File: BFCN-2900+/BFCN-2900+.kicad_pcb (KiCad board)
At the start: 2 copper layers, 60 x 30 mm, 7 parts, among them U1 BFCN-2900+, X1 SMA-BU, X2 SMA-BU

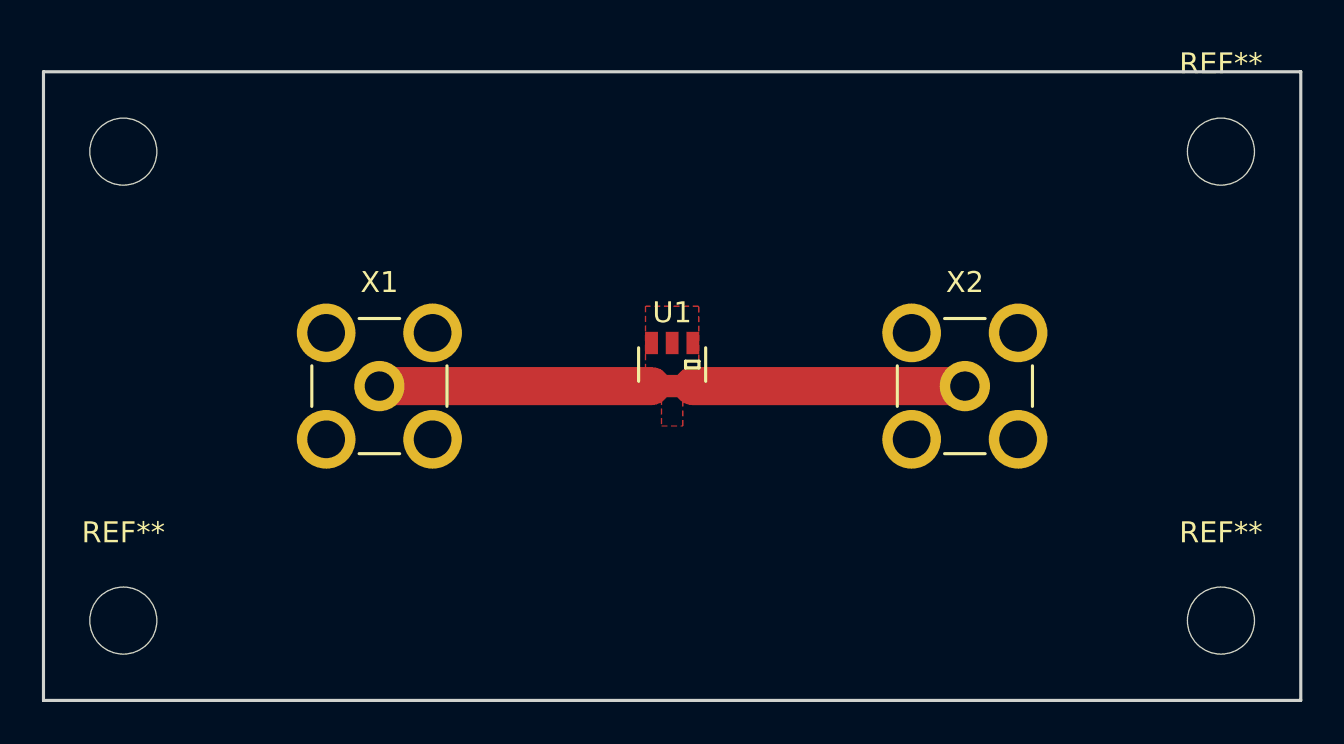
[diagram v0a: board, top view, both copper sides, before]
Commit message: BFCN-2900+: Removed thermals
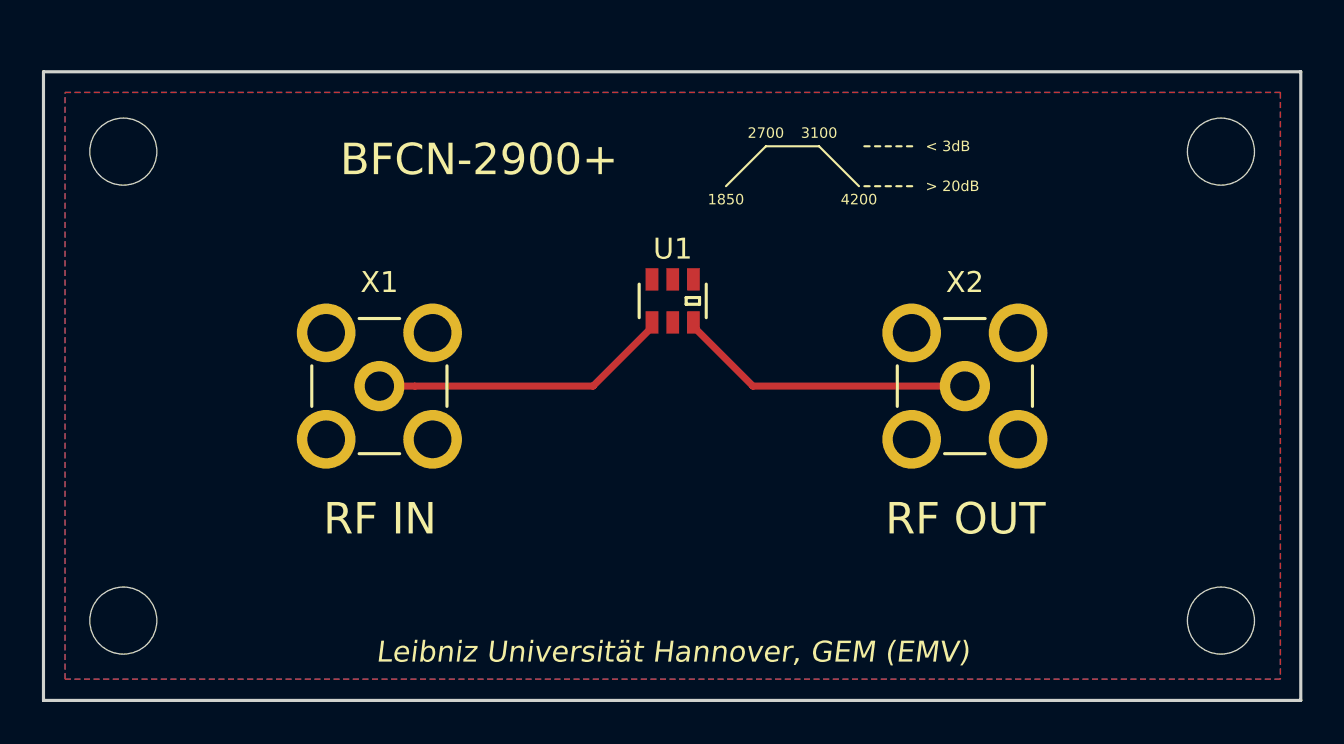
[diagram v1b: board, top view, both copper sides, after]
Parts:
- moved U1 3.04 mm to (120.0, 100.9)
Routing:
- net Net-(U1-Pad1): track 13.0 -> 14.4 mm
- net Net-(U1-Pad3): track 13.0 -> 14.3 mm
- added copper zone on B.Cu, net GNDA
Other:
- net class 50Ohm: clearance 0.1 -> 0.2; trace_width 1.82 -> 0.336; via_dia 0.6 -> 0.4; via_drill 0.4 -> 0.3
- net class Default: clearance 0.2 -> 0.1; trace_width 0.25 -> 0.15; via_dia 0.6 -> 0.4; via_drill 0.4 -> 0.3
- rule trace_clearance: 0.2 -> 0.1
- rule trace_min: 0.2 -> 0.15
- board text added: "1850"
- board text added: "2700"
- board text added: "3100"
- board text added: "4200"
- board text added: "< 3dB"
- board text added: "> 20dB"
- board text added: "BFCN-2900+"
- board text added: "Leibniz Universität Hannover, GEM (EMV)"
- board text added: "RF IN"
- board text added: "RF OUT"

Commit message: BFCN-2900+: Some vias, new footprints
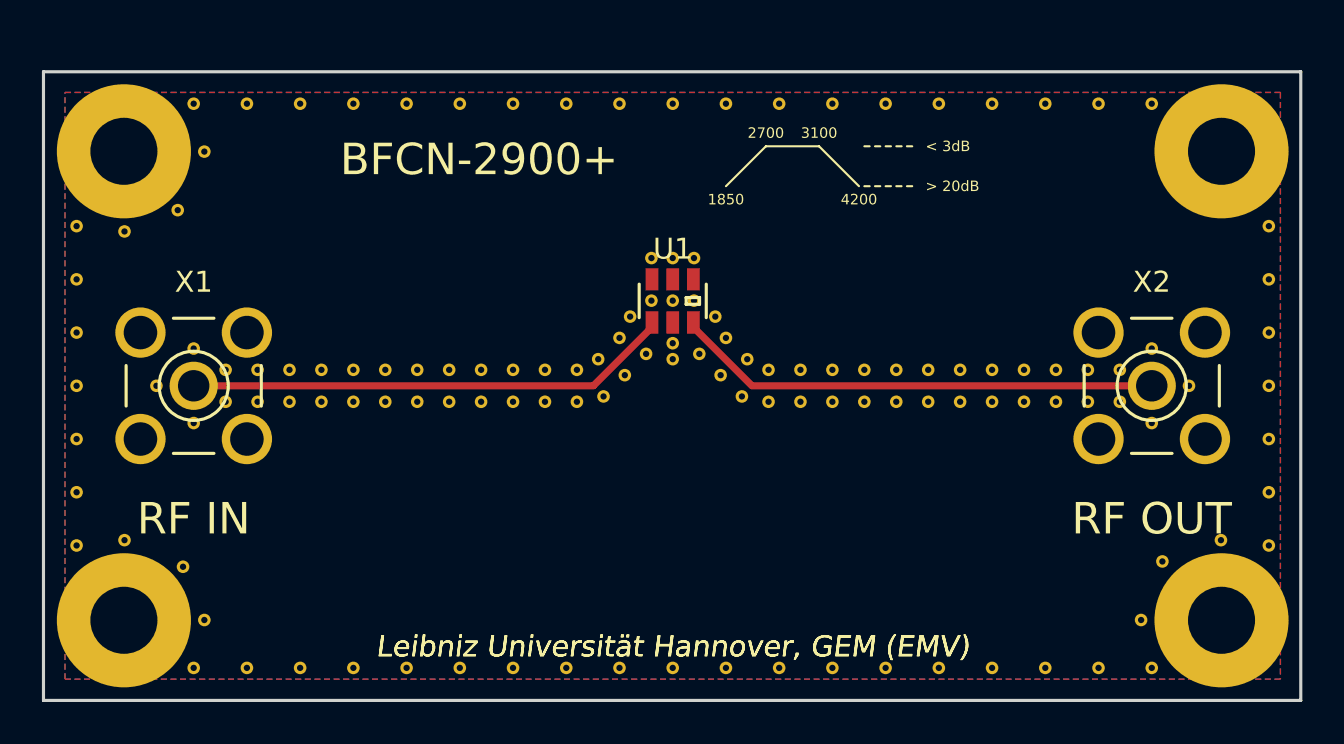
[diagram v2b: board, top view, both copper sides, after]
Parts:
- removed the REF** at (146.2, 93.8)
- removed the REF** at (146.2, 116.2)
- removed the REF** at (93.8, 93.8)
- removed the REF** at (93.8, 116.2)
- added REF**: VIA-0.3, JueVias:VIA-0.3, F.Cu at (121.0, 100.9)
- added REF**: VIA-0.3, JueVias:VIA-0.3, F.Cu at (119.0, 98.9)
- added REF**: VIA-0.3, JueVias:VIA-0.3, F.Cu at (120.0, 98.9)
- added REF**: MountingHole_3.2mm_M3_Pad, Mounting_Holes:MountingHole_3.2mm_M3_Pad, F.Cu at (93.8, 93.8)
- added REF**: MountingHole_3.2mm_M3_Pad, Mounting_Holes:MountingHole_3.2mm_M3_Pad, F.Cu at (146.2, 116.2)
- added REF**: MountingHole_3.2mm_M3_Pad, Mounting_Holes:MountingHole_3.2mm_M3_Pad, F.Cu at (93.8, 116.2)
- added REF**: MountingHole_3.2mm_M3_Pad, Mounting_Holes:MountingHole_3.2mm_M3_Pad, F.Cu at (146.2, 93.8)
- added REF**: VIA-0.3, JueVias:VIA-0.3, F.Cu at (120.0, 100.9)
- added REF**: VIA-0.3, JueVias:VIA-0.3, F.Cu at (119.0, 100.9)
- added REF**: VIA-0.3, JueVias:VIA-0.3, F.Cu at (97.2, 106.8)
- added REF**: VIA-0.3, JueVias:VIA-0.3, F.Cu at (95.4, 105.0)
- added REF**: VIA-0.3, JueVias:VIA-0.3, F.Cu at (97.2, 103.2)
- added REF**: VIA-0.3, JueVias:VIA-0.3, F.Cu at (98.7, 104.2)
- added REF**: VIA-0.3, JueVias:VIA-0.3, F.Cu at (120.0, 103.7)
- added REF**: VIA-0.3, JueVias:VIA-0.3, F.Cu at (120.0, 103.0)
- added REF**: VIA-0.3, JueVias:VIA-0.3, F.Cu at (121.0, 98.9)
- added REF**101: VIA-0.3, JueVias:VIA-0.3, F.Cu at (138.3, 105.7)
- added REF**101: VIA-0.3, JueVias:VIA-0.3, F.Cu at (138.3, 104.2)
- added REF**101: VIA-0.3, JueVias:VIA-0.3, F.Cu at (112.4, 104.2)
- added REF**101: VIA-0.3, JueVias:VIA-0.3, F.Cu at (112.4, 105.7)
- added REF**11: VIA-0.3, JueVias:VIA-0.3, F.Cu at (142.9, 106.8)
- added REF**11: VIA-0.3, JueVias:VIA-0.3, F.Cu at (115.5, 105.7)
- added REF**11: VIA-0.3, JueVias:VIA-0.3, F.Cu at (113.9, 105.7)
- added REF**11: VIA-0.3, JueVias:VIA-0.3, F.Cu at (98.7, 105.7)
- added REF**11: VIA-0.3, JueVias:VIA-0.3, F.Cu at (144.7, 105.0)
- added REF**11: VIA-0.3, JueVias:VIA-0.3, F.Cu at (142.9, 103.2)
- added REF**11: VIA-0.3, JueVias:VIA-0.3, F.Cu at (139.8, 105.7)
- added REF**11: VIA-0.3, JueVias:VIA-0.3, F.Cu at (141.4, 105.7)
- added REF**11: VIA-0.3, JueVias:VIA-0.3, F.Cu at (141.4, 104.2)
- added REF**11: VIA-0.3, JueVias:VIA-0.3, F.Cu at (139.8, 104.2)
- added REF**11: VIA-0.3, JueVias:VIA-0.3, F.Cu at (115.5, 104.2)
- added REF**11: VIA-0.3, JueVias:VIA-0.3, F.Cu at (113.9, 104.2)
- added REF**1101: VIA-0.3, JueVias:VIA-0.3, F.Cu at (120.0, 118.4)
- added REF**1101: VIA-0.3, JueVias:VIA-0.3, F.Cu at (120.0, 91.5)
- added REF**111: VIA-0.3, JueVias:VIA-0.3, F.Cu at (97.2, 118.4)
- added REF**111: VIA-0.3, JueVias:VIA-0.3, F.Cu at (97.2, 91.5)
- added REF**1111: VIA-0.3, JueVias:VIA-0.3, F.Cu at (96.7, 113.6)
- added REF**1111: VIA-0.3, JueVias:VIA-0.3, F.Cu at (122.6, 91.5)
- added REF**1111: VIA-0.3, JueVias:VIA-0.3, F.Cu at (97.7, 116.2)
- added REF**1111: VIA-0.3, JueVias:VIA-0.3, F.Cu at (93.9, 112.4)
- added REF**1111: VIA-0.3, JueVias:VIA-0.3, F.Cu at (93.9, 97.6)
- added REF**1111: VIA-0.3, JueVias:VIA-0.3, F.Cu at (96.4, 96.6)
- added REF**1111: VIA-0.3, JueVias:VIA-0.3, F.Cu at (97.7, 93.8)
- added REF**1111: VIA-0.3, JueVias:VIA-0.3, F.Cu at (148.5, 97.4)
- added REF**1111: VIA-0.3, JueVias:VIA-0.3, F.Cu at (91.6, 97.4)
- added REF**1111: VIA-0.3, JueVias:VIA-0.3, F.Cu at (122.6, 118.4)
- added REF**1112: VIA-0.3, JueVias:VIA-0.3, F.Cu at (148.5, 99.9)
- added REF**1112: VIA-0.3, JueVias:VIA-0.3, F.Cu at (91.6, 99.9)
- added REF**1113: VIA-0.3, JueVias:VIA-0.3, F.Cu at (148.5, 102.4)
- added REF**1113: VIA-0.3, JueVias:VIA-0.3, F.Cu at (91.6, 102.4)
- added REF**1114: VIA-0.3, JueVias:VIA-0.3, F.Cu at (148.5, 105.0)
- added REF**1114: VIA-0.3, JueVias:VIA-0.3, F.Cu at (91.6, 105.0)
- added REF**1115: VIA-0.3, JueVias:VIA-0.3, F.Cu at (148.5, 107.5)
- added REF**1115: VIA-0.3, JueVias:VIA-0.3, F.Cu at (91.6, 107.5)
- added REF**1116: VIA-0.3, JueVias:VIA-0.3, F.Cu at (148.5, 110.1)
- added REF**1116: VIA-0.3, JueVias:VIA-0.3, F.Cu at (91.6, 110.1)
- added REF**1117: VIA-0.3, JueVias:VIA-0.3, F.Cu at (148.5, 112.6)
- added REF**1117: VIA-0.3, JueVias:VIA-0.3, F.Cu at (91.6, 112.6)
- added REF**1121: VIA-0.3, JueVias:VIA-0.3, F.Cu at (125.1, 118.4)
- added REF**1121: VIA-0.3, JueVias:VIA-0.3, F.Cu at (125.1, 91.5)
- added REF**1131: VIA-0.3, JueVias:VIA-0.3, F.Cu at (127.6, 118.4)
- added REF**1131: VIA-0.3, JueVias:VIA-0.3, F.Cu at (127.6, 91.5)
- added REF**1141: VIA-0.3, JueVias:VIA-0.3, F.Cu at (130.2, 118.4)
- added REF**1141: VIA-0.3, JueVias:VIA-0.3, F.Cu at (130.2, 91.5)
- added REF**1151: VIA-0.3, JueVias:VIA-0.3, F.Cu at (132.7, 118.4)
- added REF**1151: VIA-0.3, JueVias:VIA-0.3, F.Cu at (132.7, 91.5)
- added REF**1161: VIA-0.3, JueVias:VIA-0.3, F.Cu at (135.3, 118.4)
- added REF**1161: VIA-0.3, JueVias:VIA-0.3, F.Cu at (135.3, 91.5)
- added REF**1171: VIA-0.3, JueVias:VIA-0.3, F.Cu at (137.8, 118.4)
- added REF**1171: VIA-0.3, JueVias:VIA-0.3, F.Cu at (137.8, 91.5)
- added REF**1181: VIA-0.3, JueVias:VIA-0.3, F.Cu at (140.3, 118.4)
- added REF**1181: VIA-0.3, JueVias:VIA-0.3, F.Cu at (140.3, 91.5)
- added REF**1191: VIA-0.3, JueVias:VIA-0.3, F.Cu at (146.2, 112.4)
- added REF**1191: VIA-0.3, JueVias:VIA-0.3, F.Cu at (143.4, 113.4)
- added REF**1191: VIA-0.3, JueVias:VIA-0.3, F.Cu at (142.4, 116.2)
- added REF**1191: VIA-0.3, JueVias:VIA-0.3, F.Cu at (142.9, 118.4)
- added REF**1191: VIA-0.3, JueVias:VIA-0.3, F.Cu at (142.9, 91.5)
- added REF**121: VIA-0.3, JueVias:VIA-0.3, F.Cu at (99.7, 118.4)
- added REF**121: VIA-0.3, JueVias:VIA-0.3, F.Cu at (99.7, 91.5)
- added REF**131: VIA-0.3, JueVias:VIA-0.3, F.Cu at (102.2, 118.4)
- added REF**131: VIA-0.3, JueVias:VIA-0.3, F.Cu at (102.2, 91.5)
- added REF**141: VIA-0.3, JueVias:VIA-0.3, F.Cu at (104.8, 118.4)
- added REF**141: VIA-0.3, JueVias:VIA-0.3, F.Cu at (104.8, 91.5)
- added REF**151: VIA-0.3, JueVias:VIA-0.3, F.Cu at (107.3, 118.4)
- added REF**151: VIA-0.3, JueVias:VIA-0.3, F.Cu at (107.3, 91.5)
- added REF**161: VIA-0.3, JueVias:VIA-0.3, F.Cu at (109.9, 118.4)
- added REF**161: VIA-0.3, JueVias:VIA-0.3, F.Cu at (109.9, 91.5)
- added REF**171: VIA-0.3, JueVias:VIA-0.3, F.Cu at (112.4, 118.4)
- added REF**171: VIA-0.3, JueVias:VIA-0.3, F.Cu at (112.4, 91.5)
- added REF**181: VIA-0.3, JueVias:VIA-0.3, F.Cu at (114.9, 118.4)
- added REF**181: VIA-0.3, JueVias:VIA-0.3, F.Cu at (114.9, 91.5)
- added REF**191: VIA-0.3, JueVias:VIA-0.3, F.Cu at (117.5, 118.4)
- added REF**191: VIA-0.3, JueVias:VIA-0.3, F.Cu at (117.5, 91.5)
- added REF**21: VIA-0.3, JueVias:VIA-0.3, F.Cu at (116.7, 105.5)
- added REF**21: VIA-0.3, JueVias:VIA-0.3, F.Cu at (122.1, 101.7)
- added REF**21: VIA-0.3, JueVias:VIA-0.3, F.Cu at (122.6, 102.7)
- added REF**21: VIA-0.3, JueVias:VIA-0.3, F.Cu at (123.6, 103.7)
- added REF**21: VIA-0.3, JueVias:VIA-0.3, F.Cu at (124.6, 105.7)
- added REF**21: VIA-0.3, JueVias:VIA-0.3, F.Cu at (126.1, 105.7)
- added REF**21: VIA-0.3, JueVias:VIA-0.3, F.Cu at (124.6, 104.2)
- added REF**21: VIA-0.3, JueVias:VIA-0.3, F.Cu at (126.1, 104.2)
- added REF**21: VIA-0.3, JueVias:VIA-0.3, F.Cu at (100.2, 104.2)
- added REF**21: VIA-0.3, JueVias:VIA-0.3, F.Cu at (100.2, 105.7)
- added REF**21: VIA-0.3, JueVias:VIA-0.3, F.Cu at (117.7, 104.5)
- added REF**21: VIA-0.3, JueVias:VIA-0.3, F.Cu at (118.8, 103.5)
- added REF**21: VIA-0.3, JueVias:VIA-0.3, F.Cu at (116.5, 103.7)
- added REF**21: VIA-0.3, JueVias:VIA-0.3, F.Cu at (117.5, 102.7)
- added REF**21: VIA-0.3, JueVias:VIA-0.3, F.Cu at (118.0, 101.7)
- added REF**21: VIA-0.3, JueVias:VIA-0.3, F.Cu at (121.3, 103.5)
- added REF**21: VIA-0.3, JueVias:VIA-0.3, F.Cu at (122.3, 104.5)
- added REF**21: VIA-0.3, JueVias:VIA-0.3, F.Cu at (123.3, 105.5)
- added REF**31: VIA-0.3, JueVias:VIA-0.3, F.Cu at (127.6, 105.7)
- added REF**31: VIA-0.3, JueVias:VIA-0.3, F.Cu at (127.6, 104.2)
- added REF**31: VIA-0.3, JueVias:VIA-0.3, F.Cu at (101.7, 104.2)
- added REF**31: VIA-0.3, JueVias:VIA-0.3, F.Cu at (101.7, 105.7)
- added REF**41: VIA-0.3, JueVias:VIA-0.3, F.Cu at (129.2, 105.7)
- added REF**41: VIA-0.3, JueVias:VIA-0.3, F.Cu at (129.2, 104.2)
- added REF**41: VIA-0.3, JueVias:VIA-0.3, F.Cu at (103.3, 104.2)
- added REF**41: VIA-0.3, JueVias:VIA-0.3, F.Cu at (103.3, 105.7)
- added REF**51: VIA-0.3, JueVias:VIA-0.3, F.Cu at (130.7, 105.7)
- added REF**51: VIA-0.3, JueVias:VIA-0.3, F.Cu at (130.7, 104.2)
- added REF**51: VIA-0.3, JueVias:VIA-0.3, F.Cu at (104.8, 104.2)
- added REF**51: VIA-0.3, JueVias:VIA-0.3, F.Cu at (104.8, 105.7)
- added REF**61: VIA-0.3, JueVias:VIA-0.3, F.Cu at (132.2, 105.7)
- added REF**61: VIA-0.3, JueVias:VIA-0.3, F.Cu at (132.2, 104.2)
- added REF**61: VIA-0.3, JueVias:VIA-0.3, F.Cu at (106.3, 104.2)
- added REF**61: VIA-0.3, JueVias:VIA-0.3, F.Cu at (106.3, 105.7)
- added REF**71: VIA-0.3, JueVias:VIA-0.3, F.Cu at (133.7, 105.7)
- added REF**71: VIA-0.3, JueVias:VIA-0.3, F.Cu at (133.7, 104.2)
- added REF**71: VIA-0.3, JueVias:VIA-0.3, F.Cu at (107.8, 104.2)
- added REF**71: VIA-0.3, JueVias:VIA-0.3, F.Cu at (107.8, 105.7)
- added REF**81: VIA-0.3, JueVias:VIA-0.3, F.Cu at (135.3, 105.7)
- added REF**81: VIA-0.3, JueVias:VIA-0.3, F.Cu at (135.3, 104.2)
- added REF**81: VIA-0.3, JueVias:VIA-0.3, F.Cu at (109.4, 104.2)
- added REF**81: VIA-0.3, JueVias:VIA-0.3, F.Cu at (109.4, 105.7)
- added REF**91: VIA-0.3, JueVias:VIA-0.3, F.Cu at (136.8, 105.7)
- added REF**91: VIA-0.3, JueVias:VIA-0.3, F.Cu at (136.8, 104.2)
- added REF**91: VIA-0.3, JueVias:VIA-0.3, F.Cu at (110.9, 104.2)
- added REF**91: VIA-0.3, JueVias:VIA-0.3, F.Cu at (110.9, 105.7)
- X1, X2: value SMA-BU -> SMA-F; footprint MiniCircuits:SMA-BU-P -> JueConnectors:SMA-F-THT
- moved X2 8.92 mm to (142.9, 105.0)
- moved X1 8.86 mm to (97.2, 105.0)
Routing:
- net (no net): track 180.0 -> 210.0 mm
- net Net-(U1-Pad3): track 14.3 -> 23.3 mm
- net Net-(U1-Pad1): track 14.4 -> 23.3 mm
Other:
- rule pad_to_mask_clearance: 0.2 -> 0.127

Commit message: BFCN-2900+: Added some vias
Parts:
- added REF**1191: VIA-0.3, JueVias:VIA-0.3, F.Cu at (143.4, 96.6)
- added REF**1191: VIA-0.3, JueVias:VIA-0.3, F.Cu at (146.2, 97.6)
- added REF**1191: VIA-0.3, JueVias:VIA-0.3, F.Cu at (142.4, 93.8)
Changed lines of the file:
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@@
 (kicad_pcb (version 4) (host pcbnew 4.0.2+e4-6225~38~ubuntu15.10.1-stable)
   (general
-    (links 87)
+    (links 148)
     (no_connects 0)
-    (area 82.420143 88.471 185.643002 133.941002)
+    (area 82.420143 88.471 185.643002 121.351)
     (thickness 1.6)
     (drawings 28)
     (tracks 10)
     (zones 0)
-    (modules 142)
+    (modules 145)
     (nets 4)
   )
@@
   )
   (module JueVias:VIA-0.3 (layer F.Cu)
+    (at 143.396 96.604)
+    (fp_text reference REF**1191 (at 0 -1) (layer F.SilkS) hide
+      (effects (font (size 1 1) (thickness 0.15)))
+    )
+    (fp_text value VIA-0.3 (at 0 1) (layer F.Fab) hide
+      (effects (font (size 1 1) (thickness 0.15)))
+    )
+    (pad 1 thru_hole circle (at 0 0) (size 0.6 0.6) (drill 0.3) (layers *.Cu)
+      (net 2 GNDA))
+  )
+  (module JueVias:VIA-0.3 (layer F.Cu)
+    (at 146.19 97.62)
+    (fp_text reference REF**1191 (at 0 -1) (layer F.SilkS) hide
+      (effects (font (size 1 1) (thickness 0.15)))
+    )
+    (fp_text value VIA-0.3 (at 0 1) (layer F.Fab) hide
+      (effects (font (size 1 1) (thickness 0.15)))
+    )
+    (pad 1 thru_hole circle (at 0 0) (size 0.6 0.6) (drill 0.3) (layers *.Cu)
+      (net 2 GNDA))
+  )
+  (module JueVias:VIA-0.3 (layer F.Cu)
+    (at 142.38 93.81)
+    (fp_text reference REF**1191 (at 0 -1) (layer F.SilkS) hide
+      (effects (font (size 1 1) (thickness 0.15)))
+    )
+    (fp_text value VIA-0.3 (at 0 1) (layer F.Fab) hide
+      (effects (font (size 1 1) (thickness 0.15)))
+    )
+    (pad 1 thru_hole circle (at 0 0) (size 0.6 0.6) (drill 0.3) (layers *.Cu)
+      (net 2 GNDA))
+  )
+  (module JueVias:VIA-0.3 (layer F.Cu)

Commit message: BFCN-2900+: Moved U1
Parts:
- removed the REF** at (120.0, 103.7)
- removed the REF** at (120.0, 103.0)
- removed the REF**21 at (116.7, 105.5)
- removed the REF**21 at (122.1, 101.7)
- removed the REF**21 at (122.6, 102.7)
- removed the REF**21 at (123.6, 103.7)
- removed the REF**21 at (117.7, 104.5)
- removed the REF**21 at (118.8, 103.5)
- removed the REF**21 at (116.5, 103.7)
- removed the REF**21 at (117.5, 102.7)
- removed the REF**21 at (118.0, 101.7)
- removed the REF**21 at (121.3, 103.5)
- removed the REF**21 at (122.3, 104.5)
- removed the REF**21 at (123.3, 105.5)
- added REF**11: VIA-0.3, JueVias:VIA-0.3, F.Cu at (123.1, 105.7)
- added REF**11: VIA-0.3, JueVias:VIA-0.3, F.Cu at (123.1, 104.2)
- added REF**11: VIA-0.3, JueVias:VIA-0.3, F.Cu at (121.0, 106.0)
- added REF**11: VIA-0.3, JueVias:VIA-0.3, F.Cu at (119.0, 106.0)
- added REF**11: VIA-0.3, JueVias:VIA-0.3, F.Cu at (120.0, 106.0)
- added REF**11: VIA-0.3, JueVias:VIA-0.3, F.Cu at (117.0, 105.7)
- added REF**11: VIA-0.3, JueVias:VIA-0.3, F.Cu at (117.0, 104.2)
- moved REF** 3.05 mm to (121.0, 104.0)
- moved REF** 3.05 mm to (120.0, 104.0)
- moved REF** 3.05 mm to (119.0, 104.0)
- moved REF** 3.05 mm to (121.0, 101.9)
- moved REF** 3.05 mm to (119.0, 101.9)
- moved REF** 3.05 mm to (120.0, 101.9)
- moved U1 3.05 mm to (120.0, 104.0)
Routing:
- net Net-(U1-Pad3): track 23.3 -> 21.9 mm
- net Net-(U1-Pad1): track 23.3 -> 21.9 mm
